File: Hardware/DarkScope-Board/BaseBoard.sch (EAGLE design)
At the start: 87 parts, among them IC1 7805DT, IC2 REG1117, IC3 7905, J1 DCJ0202, Q1 8MHz, T2 9014, U1 STM32F103CBT6, X1 TSW-102-07-G-S, X2 TSW-102-07-G-S, X3 MINI-USB-32005-301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

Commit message: CP Component Placements
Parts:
- removed JP1, JP2: (no value), pinhead:PINHD-1X2
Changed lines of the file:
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@@
 <part name="SJ4" library="jumper" library_urn="urn:adsk.eagle:library:252" deviceset="SJ" device="" package3d_urn="urn:adsk.eagle:package:15471/1"/>
 <part name="GND28" library="supply1" library_urn="urn:adsk.eagle:library:371" deviceset="GND" device=""/>
-<part name="JP1" library="pinhead" library_urn="urn:adsk.eagle:library:325" deviceset="PINHD-1X2" device="" package3d_urn="urn:adsk.eagle:package:22435/2"/>
-<part name="JP2" library="pinhead" library_urn="urn:adsk.eagle:library:325" deviceset="PINHD-1X2" device="" package3d_urn="urn:adsk.eagle:package:22435/2"/>
 <part name="R9" library="rcl" library_urn="urn:adsk.eagle:library:334" deviceset="R-US_" device="R0805" package3d_urn="urn:adsk.eagle:package:23553/2" value="180E"/>
 <part name="P+4" library="supply1" library_urn="urn:adsk.eagle:library:371" deviceset="+5V" device=""/>
@@
 <attribute name="VALUE" x="30.48" y="73.66" size="1.778" layer="96" rot="R270"/>
 </instance>
-<instance part="JP1" gate="G$1" x="29.21" y="10.16" smashed="yes">
-<attribute name="NAME" x="22.86" y="15.875" size="1.778" layer="95"/>
-<attribute name="VALUE" x="22.86" y="5.08" size="1.778" layer="96"/>
-</instance>
-<instance part="JP2" gate="G$1" x="43.18" y="10.16" smashed="yes">
-<attribute name="NAME" x="36.83" y="15.875" size="1.778" layer="95"/>
-<attribute name="VALUE" x="36.83" y="5.08" size="1.778" layer="96"/>
-</instance>
 <instance part="R9" gate="G$1" x="82.55" y="58.42" smashed="yes" rot="R180">

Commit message: UnRouted Board Bkp
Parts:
- renumbered JP4 to SIGGEN, JP5 to UART
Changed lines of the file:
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@@
 <part name="SJ5" library="jumper" library_urn="urn:adsk.eagle:library:252" deviceset="SJ" device="" package3d_urn="urn:adsk.eagle:package:15471/1"/>
 <part name="JP3" library="pinhead" library_urn="urn:adsk.eagle:library:325" deviceset="PINHD-1X4" device="" package3d_urn="urn:adsk.eagle:package:22407/2"/>
-<part name="JP4" library="pinhead" library_urn="urn:adsk.eagle:library:325" deviceset="PINHD-1X2" device="" package3d_urn="urn:adsk.eagle:package:22435/2"/>
-<part name="JP5" library="pinhead" library_urn="urn:adsk.eagle:library:325" deviceset="PINHD-1X3" device="" package3d_urn="urn:adsk.eagle:package:22458/2"/>
+<part name="SIGGEN" library="pinhead" library_urn="urn:adsk.eagle:library:325" deviceset="PINHD-1X2" device="" package3d_urn="urn:adsk.eagle:package:22435/2"/>
+<part name="UART" library="pinhead" library_urn="urn:adsk.eagle:library:325" deviceset="PINHD-1X3" device="" package3d_urn="urn:adsk.eagle:package:22458/2"/>
 <part name="GND30" library="supply1" library_urn="urn:adsk.eagle:library:371" deviceset="GND" device=""/>
 <part name="R10" library="rcl" library_urn="urn:adsk.eagle:library:334" deviceset="R-US_" device="R0805" package3d_urn="urn:adsk.eagle:package:23553/2" value="1K"/>
@@
 <attribute name="VALUE" x="45.72" y="101.6" size="1.778" layer="96" rot="MR0"/>
 </instance>
-<instance part="JP4" gate="G$1" x="39.37" y="88.9" smashed="yes" rot="R180">
+<instance part="SIGGEN" gate="G$1" x="39.37" y="88.9" smashed="yes" rot="R180">
 <attribute name="NAME" x="45.72" y="83.185" size="1.778" layer="95" rot="R180"/>
 <attribute name="VALUE" x="45.72" y="93.98" size="1.778" layer="96" rot="R180"/>
 </instance>
-<instance part="JP5" gate="A" x="39.37" y="68.58" smashed="yes" rot="R180">
+<instance part="UART" gate="A" x="39.37" y="68.58" smashed="yes" rot="R180">
 <attribute name="NAME" x="45.72" y="62.865" size="1.778" layer="95" rot="R180"/>
 <attribute name="VALUE" x="45.72" y="76.2" size="1.778" layer="96" rot="R180"/>
@@
 <net name="GND" class="0">
 <segment>
-<pinref part="JP5" gate="A" pin="1"/>
+<pinref part="UART" gate="A" pin="1"/>
 <pinref part="GND30" gate="1" pin="GND"/>
 <wire x1="41.91" y1="66.04" x2="59.69" y2="66.04" width="0.1524" layer="91"/>
@@
 <net name="N$8" class="0">
 <segment>
-<pinref part="JP5" gate="A" pin="2"/>
+<pinref part="UART" gate="A" pin="2"/>
 <pinref part="R10" gate="G$1" pin="2"/>
 <wire x1="41.91" y1="68.58" x2="62.23" y2="68.58" width="0.1524" layer="91"/>
@@
 <net name="N$18" class="0">
 <segment>
-<pinref part="JP5" gate="A" pin="3"/>
+<pinref part="UART" gate="A" pin="3"/>
 <pinref part="R11" gate="G$1" pin="2"/>
 <wire x1="41.91" y1="71.12" x2="68.58" y2="71.12" width="0.1524" layer="91"/>
@@
 <net name="N$25" class="0">
 <segment>
-<pinref part="JP4" gate="G$1" pin="2"/>
+<pinref part="SIGGEN" gate="G$1" pin="2"/>
 <pinref part="R12" gate="G$1" pin="2"/>
 <wire x1="41.91" y1="88.9" x2="53.34" y2="88.9" width="0.1524" layer="91"/>
-<pinref part="JP4" gate="G$1" pin="1"/>
+<pinref part="SIGGEN" gate="G$1" pin="1"/>
 <wire x1="53.34" y1="88.9" x2="59.69" y2="88.9" width="0.1524" layer="91"/>
 <wire x1="41.91" y1="86.36" x2="53.34" y2="86.36" width="0.1524" layer="91"/>

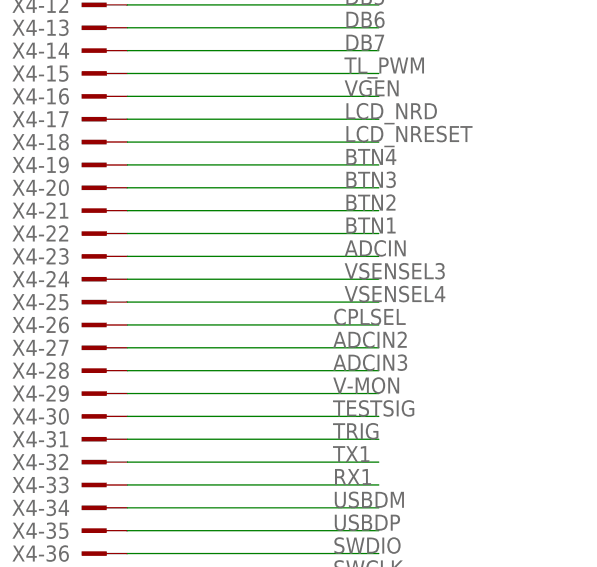
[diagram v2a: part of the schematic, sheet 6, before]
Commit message: Drafted Sch for Probe Board
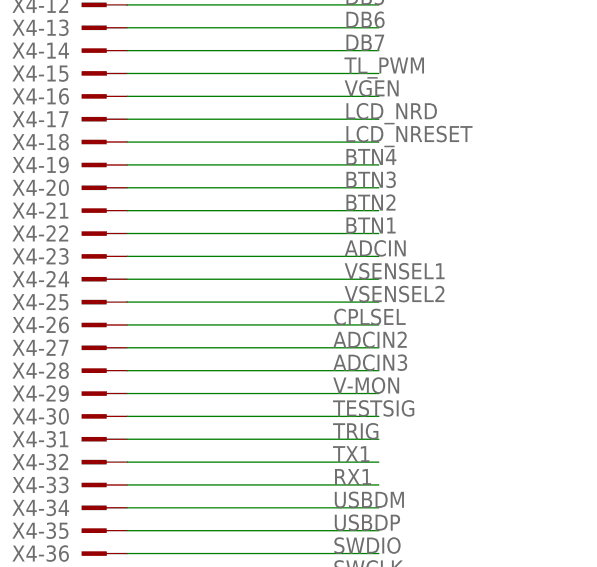
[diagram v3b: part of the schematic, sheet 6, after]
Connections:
- removed net VSENSEL3: X4-24.KL
- removed net VSENSEL4: X4-25.KL
- net VSENSEL1: now also X4-24.KL
- net VSENSEL2: now also X4-25.KL
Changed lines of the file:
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@@
 </segment>
 </net>
-<net name="VSENSEL3" class="0">
+<net name="VSENSEL1" class="0">
 <segment>
 <wire x1="38.1" y1="30.48" x2="66.04" y2="30.48" width="0.1524" layer="91"/>
@@
 </segment>
 </net>
-<net name="VSENSEL4" class="0">
+<net name="VSENSEL2" class="0">
 <segment>
 <wire x1="38.1" y1="27.94" x2="66.04" y2="27.94" width="0.1524" layer="91"/>
